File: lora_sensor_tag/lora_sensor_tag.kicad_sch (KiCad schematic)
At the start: 0 parts

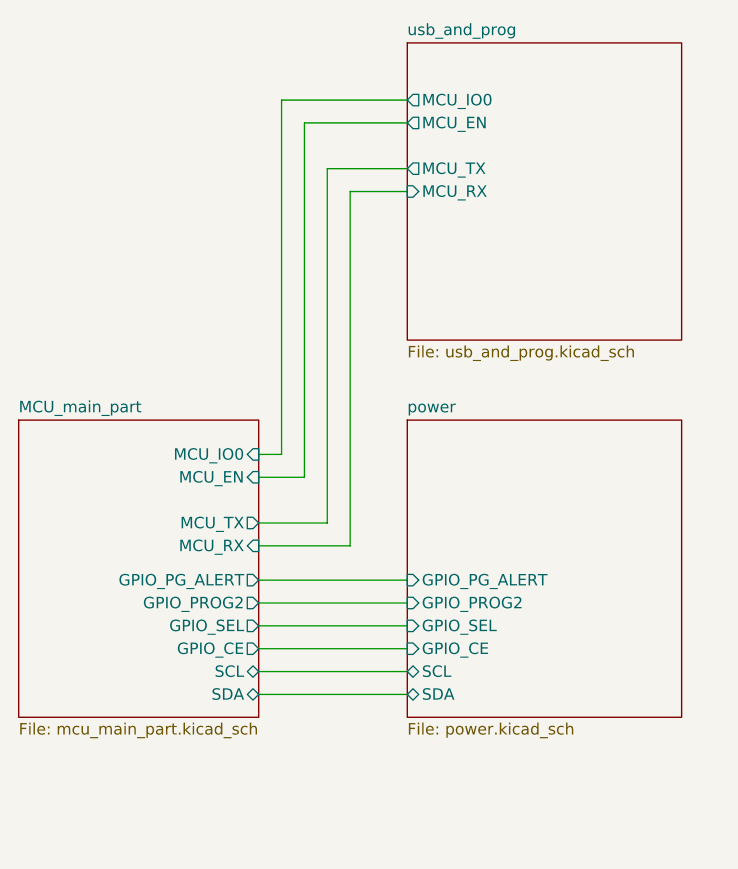
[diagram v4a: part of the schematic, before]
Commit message: Large schematic update
This commit update the following:

 - Update MCP73871 CE control schematic
 - Finished schematic development and footprint
   assignment

Signed-off-by: Volodymyr <volodymyrnoha99@gmail.com>
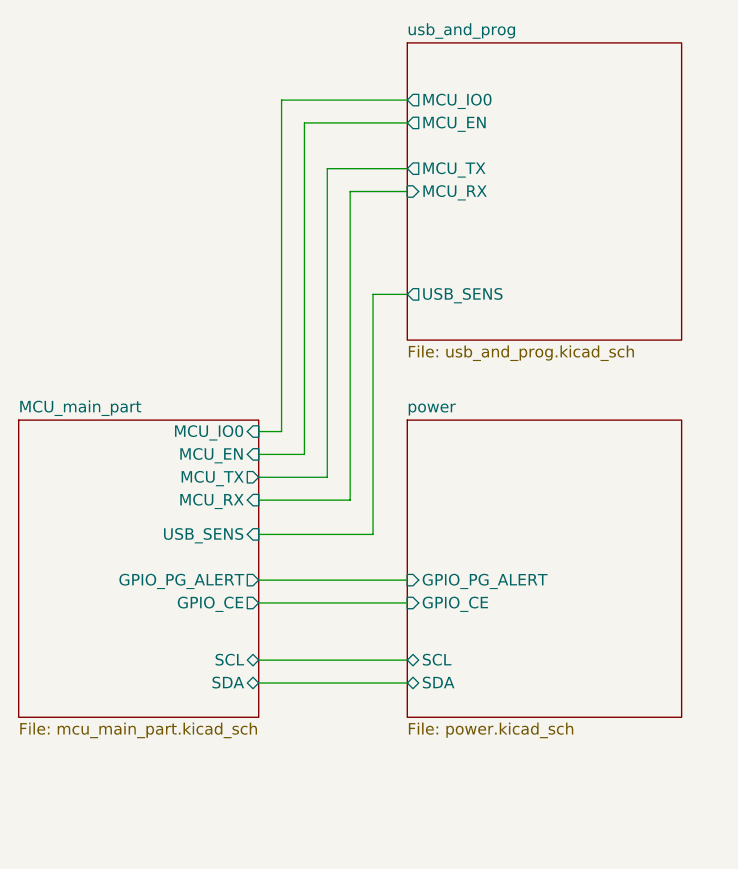
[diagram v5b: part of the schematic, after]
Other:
- sheet MCU_main_part ports: added USB_SENS; removed GPIO_PROG2, GPIO_SEL
- sheet power ports: added none; removed GPIO_PROG2, GPIO_SEL
- sheet usb_and_prog ports: added USB_SENS; removed none
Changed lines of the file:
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@@
 	(wire
 		(pts
-			(xy 137.16 97.79) (xy 132.08 97.79)
+			(xy 144.78 104.14) (xy 132.08 104.14)
+		)
+		(stroke
+			(width 0)
+			(type default)
+		)
+	)
+	(wire
+		(pts
+			(xy 137.16 95.25) (xy 132.08 95.25)
 		)
 		(stroke
@@
 	(wire
 		(pts
-			(xy 139.7 102.87) (xy 139.7 63.5)
-		)
-		(stroke
-			(width 0)
-			(type default)
-		)
-	)
-	(wire
-		(pts
-			(xy 134.62 95.25) (xy 132.08 95.25)
+			(xy 144.78 77.47) (xy 144.78 104.14)
+		)
+		(stroke
+			(width 0)
+			(type default)
+		)
+	)
+	(wire
+		(pts
+			(xy 139.7 97.79) (xy 139.7 63.5)
+		)
+		(stroke
+			(width 0)
+			(type default)
+		)
+	)
+	(wire
+		(pts
+			(xy 134.62 92.71) (xy 132.08 92.71)
 		)
 		(stroke
@@
 	(wire
 		(pts
-			(xy 132.08 121.92) (xy 148.59 121.92)
+			(xy 132.08 120.65) (xy 148.59 120.65)
 		)
 		(stroke
@@
 	(wire
 		(pts
-			(xy 132.08 114.3) (xy 148.59 114.3)
-		)
-		(stroke
-			(width 0)
-			(type default)
-		)
-	)
-	(wire
-		(pts
-			(xy 134.62 55.88) (xy 134.62 95.25)
-		)
-		(stroke
-			(width 0)
-			(type default)
-		)
-	)
-	(wire
-		(pts
-			(xy 132.08 116.84) (xy 148.59 116.84)
-		)
-		(stroke
-			(width 0)
-			(type default)
-		)
-	)
-	(wire
-		(pts
-			(xy 137.16 58.42) (xy 137.16 97.79)
-		)
-		(stroke
-			(width 0)
-			(type default)
-		)
-	)
-	(wire
-		(pts
-			(xy 132.08 105.41) (xy 142.24 105.41)
-		)
-		(stroke
-			(width 0)
-			(type default)
-		)
-	)
-	(wire
-		(pts
-			(xy 142.24 105.41) (xy 142.24 66.04)
-		)
-		(stroke
-			(width 0)
-			(type default)
-		)
-	)
-	(wire
-		(pts
-			(xy 132.08 119.38) (xy 148.59 119.38)
+			(xy 134.62 55.88) (xy 134.62 92.71)
 		)
 		(stroke
@@
 	(wire
 		(pts
-			(xy 132.08 102.87) (xy 139.7 102.87)
+			(xy 137.16 58.42) (xy 137.16 95.25)
+		)
+		(stroke
+			(width 0)
+			(type default)
+		)
+	)
+	(wire
+		(pts
+			(xy 132.08 100.33) (xy 142.24 100.33)
+		)
+		(stroke
+			(width 0)
+			(type default)
+		)
+	)
+	(wire
+		(pts
+			(xy 142.24 100.33) (xy 142.24 66.04)
+		)
+		(stroke
+			(width 0)
+			(type default)
+		)
+	)
+	(wire
+		(pts
+			(xy 132.08 118.11) (xy 148.59 118.11)
+		)
+		(stroke
+			(width 0)
+			(type default)
+		)
+	)
+	(wire
+		(pts
+			(xy 132.08 97.79) (xy 139.7 97.79)
 		)
 		(stroke
@@
 		(pts
 			(xy 132.08 109.22) (xy 148.59 109.22)
+		)
+		(stroke
+			(width 0)
+			(type default)
+		)
+	)
+	(wire
+		(pts
+			(xy 148.59 77.47) (xy 144.78 77.47)
 		)
 		(stroke
@@
 			)
 		)
-		(pin "GPIO_PROG2" output
+		(pin "MCU_RX" input
+			(at 132.08 100.33 0)
+			(effects
+				(font
+					(size 1.27 1.27)
+				)
+				(justify right)
+			)
+		)
+		(pin "MCU_TX" output
+			(at 132.08 97.79 0)
+			(effects
+				(font
+					(size 1.27 1.27)
+				)
+				(justify right)
+			)
+		)
+		(pin "SCL" bidirectional
+			(at 132.08 118.11 0)
+			(effects
+				(font
+					(size 1.27 1.27)
+				)
+				(justify right)
+			)
+		)
+		(pin "SDA" bidirectional
+			(at 132.08 120.65 0)
+			(effects
+				(font
+					(size 1.27 1.27)
+				)
+				(justify right)
+			)
+		)
+		(pin "MCU_EN" input
+			(at 132.08 95.25 0)
+			(effects
+				(font
+					(size 1.27 1.27)
+				)
+				(justify right)
+			)
+		)
+		(pin "MCU_IO0" input
+			(at 132.08 92.71 0)
+			(effects
+				(font
+					(size 1.27 1.27)
+				)
+				(justify right)
+			)
+		)
+		(pin "GPIO_CE" output
 			(at 132.08 111.76 0)
 			(effects
@@
 			)
 		)
-		(pin "GPIO_SEL" output
-			(at 132.08 114.3 0)
-			(effects
-				(font
-					(size 1.27 1.27)
-				)
-				(justify right)
-			)
-		)
-		(pin "MCU_RX" input
-			(at 132.08 105.41 0)
-			(effects
-				(font
-					(size 1.27 1.27)
-				)
-				(justify right)
-			)
-		)
-		(pin "MCU_TX" output
-			(at 132.08 102.87 0)
-			(effects
-				(font
-					(size 1.27 1.27)
-				)
-				(justify right)
-			)
-		)
-		(pin "SCL" bidirectional
-			(at 132.08 119.38 0)
-			(effects
-				(font
-					(size 1.27 1.27)
-				)
-				(justify right)
-			)
-		)
-		(pin "SDA" bidirectional
-			(at 132.08 121.92 0)
-			(effects
-				(font
-					(size 1.27 1.27)
-				)
-				(justify right)
-			)
-		)
-		(pin "MCU_EN" input
-			(at 132.08 97.79 0)
-			(effects
-				(font
-					(size 1.27 1.27)
-				)
-				(justify right)
-			)
-		)
-		(pin "MCU_IO0" input
-			(at 132.08 95.25 0)
-			(effects
-				(font
-					(size 1.27 1.27)
-				)
-				(justify right)
-			)
-		)
-		(pin "GPIO_CE" output
-			(at 132.08 116.84 0)
+		(pin "USB_SENS" input
+			(at 132.08 104.14 0)
 			(effects
 				(font
@@
 			)
 		)
-		(pin "GPIO_PROG2" input
-			(at 148.59 111.76 180)
-			(effects
-				(font
-					(size 1.27 1.27)
-				)
-				(justify left)
-			)
-		)
 		(pin "GPIO_PG_ALERT" input
 			(at 148.59 109.22 180)
@@
 			)
 		)
-		(pin "GPIO_SEL" input
-			(at 148.59 114.3 180)
-			(effects
-				(font
-					(size 1.27 1.27)
-				)
-				(justify left)
-			)
-		)
 		(pin "SCL" bidirectional
-			(at 148.59 119.38 180)
+			(at 148.59 118.11 180)
 			(effects
 				(font
@@
 		)
 		(pin "SDA" bidirectional
-			(at 148.59 121.92 180)
+			(at 148.59 120.65 180)
 			(effects
 				(font
@@
 		)
 		(pin "GPIO_CE" input
-			(at 148.59 116.84 180)
+			(at 148.59 111.76 180)
 			(effects
 				(font
@@
 			(effects
 				(font
+					(size 1.27 1.27)
+				)
+				(justify left)
+			)
+		)
+		(pin "USB_SENS" output
+			(at 148.59 77.47 180)
+			(effects
+				(font
